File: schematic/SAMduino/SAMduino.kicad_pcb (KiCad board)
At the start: 4 copper layers, 100 x 100 mm, 96 parts, among them IC1 ATSAMV71N21B-AABT, IC2 MCP1703AT-5002E_CB, IC3 NCP5501DT33RKG, IC4 SST26VF064B-104V_SM, IC5 MCP2221-I_SL, IC6 MCP2542FD-E_SN, J1 Barrel_Jack_Switch, J10 Conn_02x11_Odd_Even, J11 Conn_02x09_Odd_Even, J12 Conn_02x09_Odd_Even, J13 Conn_01x02, J14 Conn_02x02_Odd_Even, J15 Conn_02x03_Odd_Even, J16 Conn_01x02, J17 Conn_02x03_Odd_Even, J18 Conn_02x02_Odd_Even, J19 Conn_02x03_Odd_Even, J2 Conn_02x02_Odd_Even, J20 Conn_01x08, J3 USB_B_Micro, J4 USB_B_Mini, J5 Conn_01x02, J6 Screw_Terminal_01x02, J7 Conn_01x02, J8 Conn_01x02, J9 Conn_02x07_Odd_Even, SW1 SW_MEC_5E, SW2 SW_MEC_5E, SW3 MCLR, SW4 ERASE, X1 AMPMAFB-12.0000T, X2 32.768 kHz 12.5 pF

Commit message: Almost routed - first attempt
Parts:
- moved D2 184.2 mm to (47.5, 145.0), turned to 180 degrees
- moved R16 148.5 mm to (42.8, 56.2), turned to 180 degrees
- moved R8 146.9 mm to (47.2, 59.1), turned to 90 degrees
- moved R17 141.5 mm to (42.8, 63.8), turned to 180 degrees
- moved R4 141.1 mm to (43.5, 122.8)
- moved C27 140.7 mm to (44.2, 116.2), turned to 90 degrees
- moved C8 138.3 mm to (78.5, 111.5), turned to 270 degrees
- moved C17 137.4 mm to (72.0, 103.5), turned to 180 degrees
- moved C23 137.2 mm to (70.5, 96.2)
- moved C19 131.7 mm to (72.0, 106.5), turned to 180 degrees
- moved C16 131.4 mm to (72.0, 98.8)
- moved R1 130.1 mm to (69.8, 92.0), turned to 180 degrees
- moved C6 128.4 mm to (72.0, 104.5), turned to 180 degrees
- moved C4 128.2 mm to (69.8, 90.5), turned to 180 degrees
- moved C22 126.9 mm to (72.5, 96.2), turned to 180 degrees
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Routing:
- net NRST: track 0.00 -> 96.9 mm, vias 0 -> 1
- net URXD0: track 0.00 -> 93.9 mm, vias 0 -> 2
- net VDDOUT: track 0.00 -> 88.3 mm, vias 0 -> 4
- net VIN: track 20.1 -> 106.3 mm
- net DAC0: track 0.00 -> 61.5 mm, vias 0 -> 1
- net Button1: track 0.00 -> 58.3 mm, vias 0 -> 2
- net UTXD0: track 0.00 -> 54.5 mm
- net QCS: track 0.00 -> 52.2 mm, vias 0 -> 2
- net QIO1: track 0.00 -> 50.2 mm, vias 0 -> 2
- net GND: track 53.9 -> 102.6 mm, vias 17 -> 46
- net VCC3V3: track 18.6 -> 64.8 mm, vias 4 -> 20
- net CAN_STBY: track 0.00 -> 43.6 mm, vias 0 -> 4
- net CANTX: track 0.00 -> 41.6 mm, vias 0 -> 2
- net QIO3: track 0.00 -> 41.2 mm, vias 0 -> 2
- net SPI0_SPCK: track 0.00 -> 41.1 mm, vias 0 -> 1
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
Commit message: PCB routed - needs optimization
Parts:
- added R20: 10k, Resistor_SMD:R_0603_1608Metric, F.Cu at (63.4, 135.4)
- moved J3 105.5 mm to (37.4, 64.8), turned to 270 degrees
- moved R16 101.6 mm to (124.7, 116.4), turned to 270 degrees
- moved C20 99.2 mm to (43.4, 57.1), turned to 180 degrees
- moved D1 99.0 mm to (44.0, 61.6), turned to 270 degrees
- moved J20 94.3 mm to (128.8, 99.5), turned to 0 degrees
- moved R17 94.2 mm to (124.7, 110.5), turned to 90 degrees
- moved R2 94.2 mm to (51.5, 57.8)
- moved R3 93.1 mm to (47.9, 57.8), turned to 0 degrees
- moved R8 81.0 mm to (118.2, 98.2), turned to 0 degrees
- moved SW3 75.5 mm to (120.0, 93.8)
- moved SW4 68.5 mm to (121.2, 85.5), turned to 180 degrees
- moved R13 56.7 mm to (115.0, 86.2), turned to 90 degrees
- moved J14 23.3 mm to (123.7, 75.6)
- moved R15 22.7 mm to (129.9, 72.1)
- moved R14 21.6 mm to (119.7, 72.2)
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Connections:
- C26 pad 1: VCC3V3 -> GND
- C26 pad 2: GND -> VCC3V3
- IC5 pad 4: NRST -> Net-(IC5-Pad4)
- J6 pad 1: Net-(IC6-Pad7) -> Net-(IC6-Pad6)
- J6 pad 2: Net-(IC6-Pad6) -> Net-(IC6-Pad7)
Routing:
- net VUSB5V: track 37.3 -> 160.6 mm
- net VIN: track 106.3 -> 203.6 mm, vias 0 -> 4
- net VUSB_Detect: track 3.31 -> 68.4 mm, vias 0 -> 4
- net HSDM: track 0.00 -> 60.1 mm, vias 0 -> 2
- net HSDP: track 0.00 -> 58.9 mm, vias 0 -> 2
- net NRST: track 96.9 -> 44.2 mm, vias 1 -> 2
- net PB5: track 21.7 -> 69.8 mm, vias 0 -> 2
- net SPI0_NPCS0: track 18.8 -> 61.6 mm, vias 0 -> 1
- net SWCLK: track 4.01 -> 45.3 mm, vias 0 -> 1
- net SWDIO: track 4.00 -> 45.0 mm, vias 0 -> 2
- net ERASE: track 3.57 -> 38.7 mm, vias 0 -> 2
- net GND: track 102.6 -> 123.1 mm, vias 46 -> 44
- net TWCK0: track 39.2 -> 59.5 mm
- net TWD0: track 35.0 -> 55.0 mm
- net VDDOUT: track 88.3 -> 75.5 mm, vias 4 -> 3
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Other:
- board text added: "PD3"

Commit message: Some silkscreen done
Prior to swapping ICSP pins
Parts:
- moved R15 19.6 mm to (110.4, 71.7), turned to 180 degrees
- moved J14 17.8 mm to (105.8, 76.0)
- moved R14 9.78 mm to (110.5, 69.0), turned to 180 degrees
- moved J16 7.27 mm to (119.8, 69.2)
- moved J13 7.27 mm to (116.2, 69.2)
- moved SW3 5.98 mm to (124.7, 90.2)
- moved SW4 5.96 mm to (124.7, 80.5)
- moved J2 5.65 mm to (112.2, 130.1)
- moved D11 4.07 mm to (112.7, 141.2)
- moved D9 4.07 mm to (117.7, 141.2)
- moved R19 4.07 mm to (112.7, 145.9)
- moved R18 3.81 mm to (117.6, 145.9)
- moved J5 2.98 mm to (86.1, 145.0)
- moved R7 2.98 mm to (88.0, 141.6)
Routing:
- net GND: track 123.1 -> 113.8 mm, vias 44 -> 45
- net Net-(C7-Pad1): track 17.0 -> 9.23 mm
- net TWCK0: track 59.5 -> 51.8 mm
- net NRST: track 44.2 -> 51.2 mm
- net Net-(J16-Pad2): track 3.52 -> 10.4 mm
- net ERASE: track 38.7 -> 45.1 mm
- net Net-(IC6-Pad6): track 16.9 -> 19.6 mm
- net Net-(IC6-Pad7): track 20.1 -> 22.8 mm
- net Net-(J13-Pad2): track 4.06 -> 6.75 mm
- net TWD0: track 55.0 -> 57.2 mm
- net Button1: track 63.3 -> 64.7 mm
- net QIO0: track 31.8 -> 30.8 mm, vias 0 -> 2
- net VUSB5V: track 160.6 -> 159.9 mm
- net VIN: track 203.6 -> 204.3 mm
- net VCC3V3: track 69.1 -> 68.9 mm, vias 20 -> 21
- added copper zone on F.Cu, net GND
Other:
- outline, holes or cut-outs redrawn
- board text added: "1"
- board text added: "120 Ω"
- board text added: "2"
- board text added: "3"
- board text added: "3V3"
- board text added: "4"
- board text added: "5V"
- board text added: "AD0"
- board text added: "AD1"
- board text added: "AD2"
- board text added: "ADC/DAC"
- board text added: "CANH"
- board text added: "CANL"
- board text added: "DAC0"
- board text added: "ERASE"
- board text added: "GND"
- board text added: "JLCJLCJLCJLC"
- board text added: "Jumpers J2 - Position 1-2 = 5V from Vin Position 3-4 = 5V from USB J5 CAN termination enable J7 LED D5, D6 enable J8 LED D7, D8 enable J13, J16 TWI pullup enable"
- board text added: "MISO"
- board text added: "MOSI"
- board text added: "NPCS"
- board text added: "NRST"
- board text added: "PA15"
- board text added: "PA18"
- board text added: "PA19"
- board text added: "PA20"
- board text added: "PA21"
- board text added: "PA22"
- board text added: "PA23"
- board text added: "PA24"
- board text added: "PB0"
- board text added: "PB1"
- board text added: "PB2"
- board text added: "PB3"
- board text added: "PD0"
- board text added: "PD26"
- board text added: "PD30"
- board text added: "PD8"
- board text added: "POWER"
- board text added: "QES 2020"
- board text added: "RX"
- board text added: "RXD0"
- board text added: "SAMduino 1.0"
- board text added: "SPCK"
- board text added: "SPI0"
- board text added: "TWCK0"
- board text added: "TWD0"
- board text added: "TWI0"
- board text added: "TX"
- board text added: "TXD0"
- board text added: "UART0"
- board text added: "USART0"
- board text added: "USB"
- board text added: "Vin"

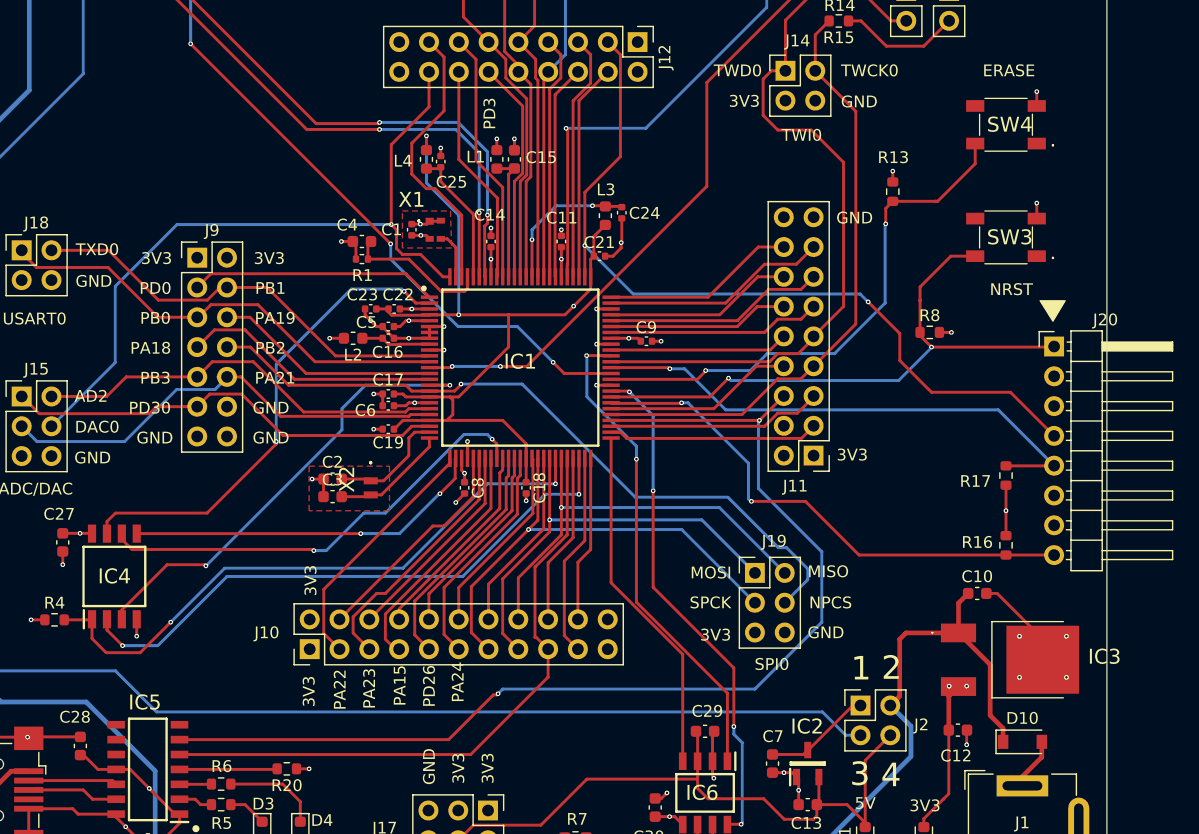
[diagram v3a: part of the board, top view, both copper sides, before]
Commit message: Swapped program header to match PicKit4
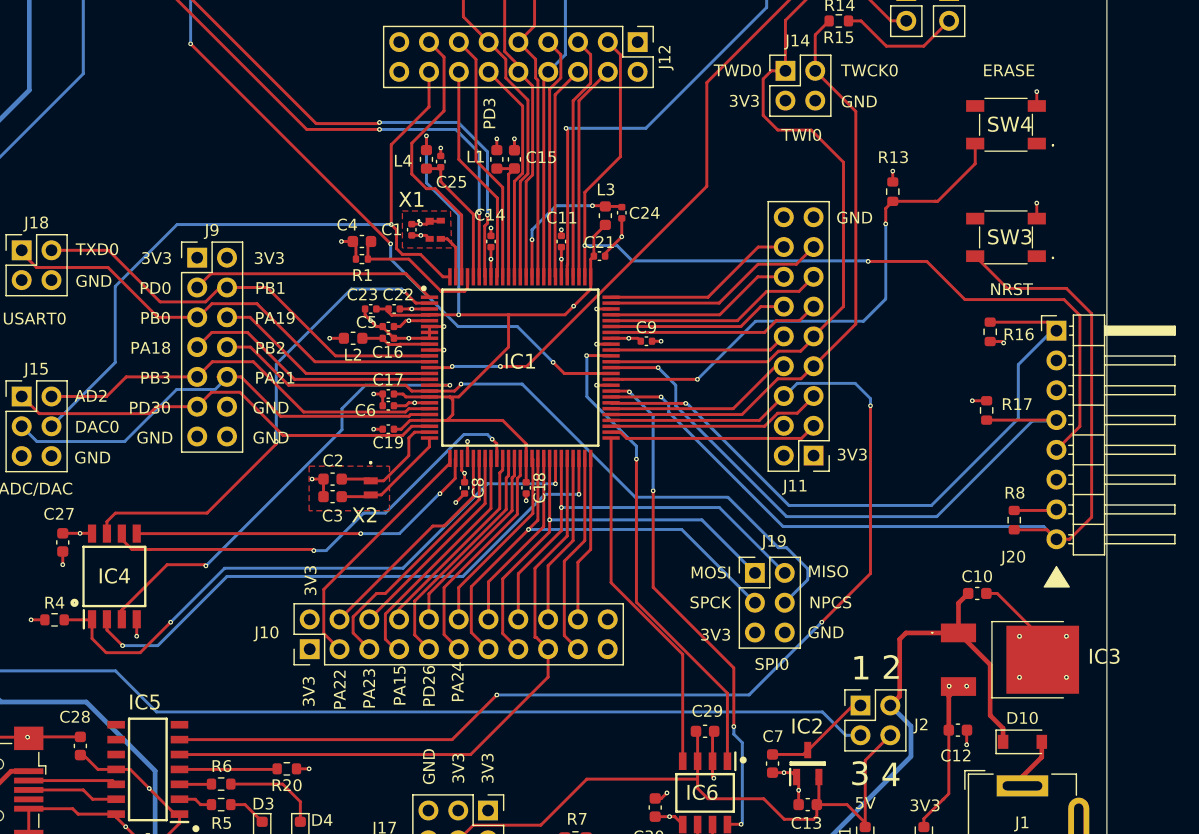
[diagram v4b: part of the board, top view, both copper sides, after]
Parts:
- moved R16 18.3 mm to (123.3, 98.2), turned to 90 degrees
- moved R8 17.5 mm to (125.3, 114.2), turned to 90 degrees
- moved R17 5.79 mm to (123.0, 104.9), turned to 270 degrees
- moved J20 1.36 mm to (128.9, 98.1)
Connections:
- J20 pad 1: NRST -> SWDIO
- J20 pad 2: VCC3V3 -> Net-(J20-Pad2)
- J20 pad 3: GND -> Net-(J20-Pad3)
- J20 pad 4: PB5 -> SWCLK
- J20 pad 5: SWCLK -> PB5
- J20 pad 6: Net-(J20-Pad6) -> GND
- J20 pad 7: Net-(J20-Pad7) -> VCC3V3
- J20 pad 8: SWDIO -> NRST
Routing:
- net NRST: track 51.2 -> 80.4 mm, vias 2 -> 1
- net SWDIO: track 45.0 -> 57.4 mm, vias 2 -> 1
- net URXD0: track 93.9 -> 103.6 mm, vias 2 -> 3
- net PB5: track 69.8 -> 79.1 mm
- net SWCLK: track 45.3 -> 53.6 mm
- net VCC3V3: track 68.9 -> 69.6 mm

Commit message: Full PCB layout
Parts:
- moved J12 2.65 mm to (93.2, 70.8)
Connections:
- SW1 pad 1: Net-(SW1-Pad1) -> Button1
- SW1 pad 4: Net-(SW1-Pad4) -> GND
- SW2 pad 1: Net-(SW2-Pad1) -> Button2
- SW2 pad 4: Net-(SW2-Pad4) -> GND
- SW3 pad 1: Net-(SW3-Pad1) -> NRST
- SW3 pad 4: Net-(SW3-Pad4) -> GND
- SW4 pad 1: Net-(SW4-Pad1) -> ERASE
- SW4 pad 4: Net-(SW4-Pad4) -> VCC3V3
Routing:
- net Button1: track 64.7 -> 71.2 mm
- net VCC3V3: track 69.6 -> 74.9 mm
- net NRST: track 80.4 -> 85.6 mm
- net GND: track 113.4 -> 118.6 mm
- net ERASE: track 45.0 -> 50.3 mm
- net PA31: track 20.9 -> 23.6 mm
- net PD3: track 19.0 -> 21.6 mm
- net PA28: track 21.1 -> 23.7 mm
- net PD2: track 21.6 -> 24.2 mm
- net PD1: track 18.9 -> 21.5 mm
- net PB8: track 23.9 -> 26.5 mm
- net PA30: track 18.3 -> 21.0 mm
- net DAC0: track 62.0 -> 64.7 mm
- net PB5: track 79.1 -> 81.7 mm
- net PD9: track 18.5 -> 21.2 mm
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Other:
- board text added: "PA0"
- board text added: "PA1"
- board text added: "PA10"
- board text added: "PA16"
- board text added: "PA2"
- board text added: "PA25"
- board text added: "PA26"
- board text added: "PA27"
- board text added: "PA28"
- board text added: "PA3"
- board text added: "PA30"
- board text added: "PA31"
- board text added: "PA4"
- board text added: "PA5"
- board text added: "PA9"
- board text added: "PB13"
- board text added: "PB4"
- board text added: "PB5"
- board text added: "PB8"
- board text added: "PD1"
- board text added: "PD10"
- board text added: "PD11"
- board text added: "PD15"
- board text added: "PD16"
- board text added: "PD17"
- board text added: "PD18"
- board text added: "PD19"
- board text added: "PD2"
- board text added: "PD20"
- board text added: "PD21"
- board text added: "PD22"
- board text added: "PD24"
- board text added: "PD25"
- board text added: "PD27"
- board text added: "PD4"
- board text added: "PD5"
- board text added: "PD6"
- board text added: "PD7"
- board text added: "PD9"
- board text added: "QES 2021"
- board text removed: "QES 2020"

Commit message: Minor fixes to PCB
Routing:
- net GND: track 118.6 -> 117.5 mm, vias 45 -> 49
- net VDDOUT: vias 3 -> 2
- net VCC3V3: vias 21 -> 22
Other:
- board text removed: "120 Ω"
